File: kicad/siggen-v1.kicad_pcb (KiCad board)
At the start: 4 copper layers, 39 x 60 mm, 121 parts, among them J1 Conn_Coaxial, J2 USB_C_Receptacle_USB2.0, J3 BNC, J5 Conn_01x06, Q1 BC857, Q2 BC847, Q3 BC857, Q4 CSD15380F3, Q5 CSD15380F3, U1 AD9954, U2 OPA859xDSG, U3 MCP2210x-SS, U4 AP62201-SOT563, U5 AP62201-SOT563, U6 TLV71x, U7 TLV71x, U8 OPA355NA, X1 ASE-xxxMHz, Y1 CSTNE12M0GH5L000R0

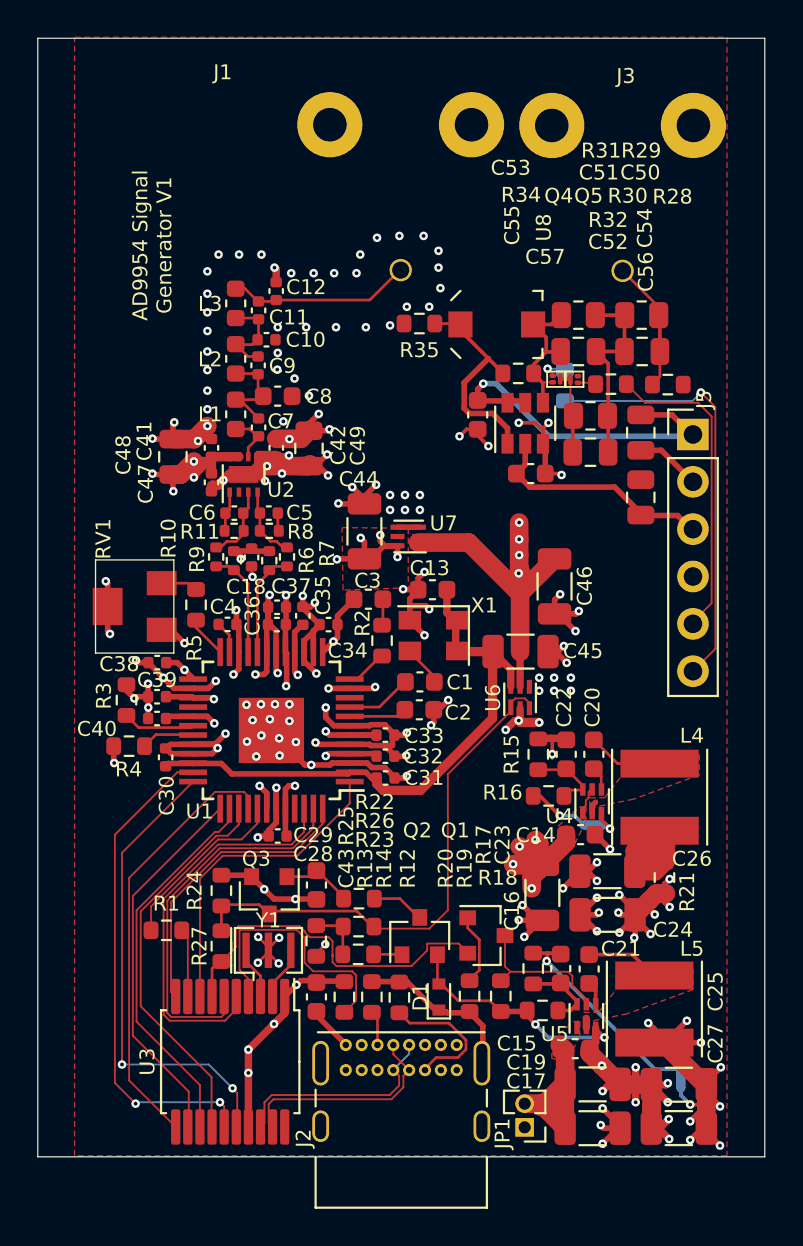
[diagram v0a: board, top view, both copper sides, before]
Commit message: removed frontent/amp test circuit
This circuit had shared the PCB for cost reasons.
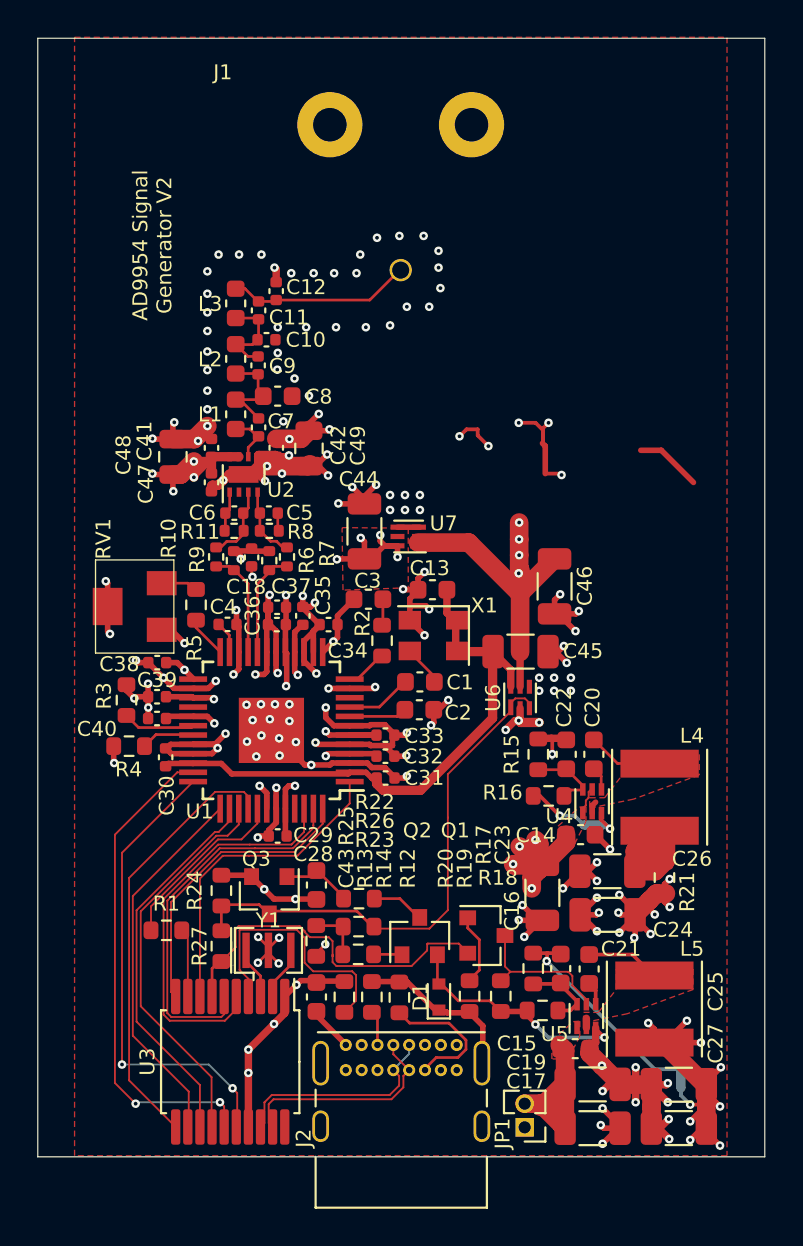
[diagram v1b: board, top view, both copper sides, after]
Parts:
- removed C50, C51: 11p, Capacitor_SMD:C_0805_2012Metric
- removed C52: 98.8p, Capacitor_SMD:C_0805_2012Metric
- removed C53: 3-10p, proj_footprints:C_Trimmer_EW_Electronics_SCG3S
- removed C54, C56: 1u, Capacitor_SMD:C_0805_2012Metric
- removed C55, C57: 100n, Capacitor_SMD:C_0603_1608Metric
- removed J3: BNC, proj_footprints:BNC_Molex_0731713150
- removed J5: Conn_01x06, Connector_PinHeader_2.54mm:PinHeader_1x06_P2.54mm_Vertical
- removed Q4, Q5: CSD15380F3, proj_footprints:FemtoFetF3
- removed R28, R35: 50, Resistor_SMD:R_0603_1608Metric
- removed R29, R31: 909k, Resistor_SMD:R_0805_2012Metric
- removed R30, R33: 100k, Resistor_SMD:R_0603_1608Metric
- removed R32: 102k, Resistor_SMD:R_0805_2012Metric
- removed R34: 1M 1%, Resistor_SMD:R_0603_1608Metric
- removed U8: OPA355NA, Package_TO_SOT_SMD:SOT-23-6
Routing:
- net CTL_2: track 23.3 -> 0.00 mm, vias 1 -> 0
- net +2V5: track 19.3 -> 0.00 mm, vias 1 -> 0
- net CTL_1: track 16.9 -> 0.00 mm
- net -2V5: track 12.7 -> 0.00 mm
- net Net-(C53-Pad1): track 12.2 -> 0.00 mm
- net Net-(C50-Pad1): track 10.8 -> 0.00 mm
- net Net-(C51-Pad1): track 8.06 -> 0.00 mm
- net Net-(C50-Pad2): track 7.29 -> 0.00 mm
- net Net-(C52-Pad1): track 4.45 -> 0.00 mm
- net Net-(Q4-Pad1): track 1.47 -> 0.00 mm, vias 1 -> 0
- net Net-(Q5-Pad1): track 0.96 -> 0.00 mm
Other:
- board text added: "AD9954 Signal Generator V2"
- board text removed: "AD9954 Signal Generator V1"

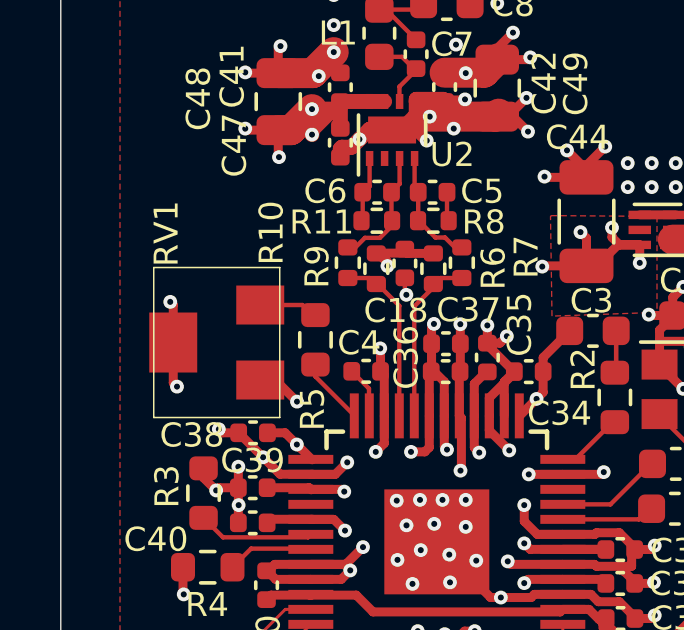
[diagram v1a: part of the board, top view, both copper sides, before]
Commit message: moved RV1 (pot) away from board edge (README.errata)
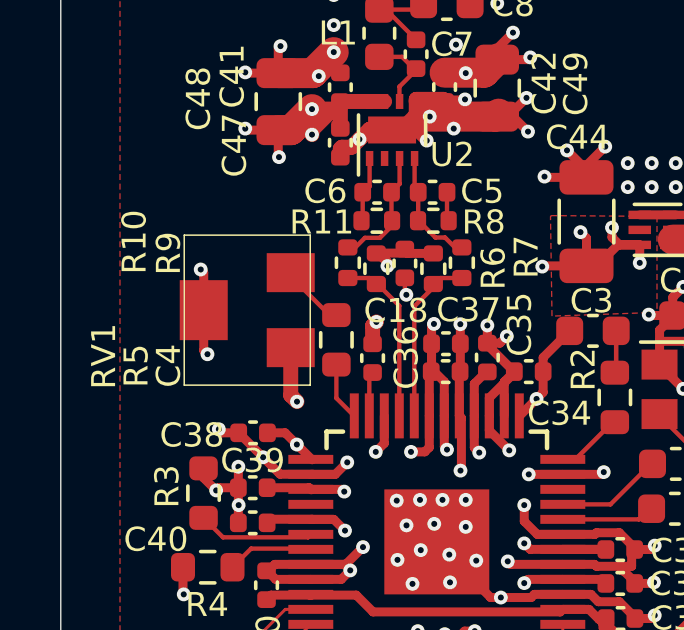
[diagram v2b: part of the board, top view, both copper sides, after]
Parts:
- moved RV1 1.48 mm to (104.2, 129.4)
- moved R5 0.70 mm to (107.2, 130.4)
- moved C4 0.49 mm to (108.4, 131.0), turned to 270 degrees
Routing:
- net GND: track 160.0 -> 158.9 mm
